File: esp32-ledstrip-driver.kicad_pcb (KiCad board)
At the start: 2 copper layers, 43 parts, among them P1 PWR, P2 LED_1, P3 LED_2, P4 LED_3, P5 LED_4, P6 RS485, Q1 FDD8880?, Q2 FDD8880?, Q3 FDD8880?, Q4 FDD8880?, Q5 FDD8880?, Q6 FDD8880?, Q7 FDD8880?, Q8 FDD8880?, U1 ESP32-WROOM-32, U2 R-78E-1.0, U3 MAX481E

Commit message: first gerbers generated
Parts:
- added C5: 20p, Capacitor_SMD:C_0603_1608Metric, F.Cu at (157.3, 81.7)
- added C6: 20p, Capacitor_SMD:C_0603_1608Metric, F.Cu at (149.7, 81.6)
- added C7: 100n, Capacitor_SMD:C_0603_1608Metric, F.Cu at (151.0, 85.8)
- added C8: 22u, Capacitor_SMD:C_0603_1608Metric, F.Cu at (161.2, 94.7)
- added D2: D_Schottky_Small, Diode_SMD:D_0603_1608Metric_Pad1.05x0.95mm_HandSolder, F.Cu at (160.4, 81.7)
- added D3: D_Schottky_Small, Diode_SMD:D_0603_1608Metric_Pad1.05x0.95mm_HandSolder, F.Cu at (151.2, 92.4)
- added D4: D_Schottky_Small, Diode_SMD:D_0603_1608Metric_Pad1.05x0.95mm_HandSolder, F.Cu at (160.5, 97.5)
- added D5: BAT54C, Package_TO_SOT_SMD:SOT-23, F.Cu at (147.3, 96.1)
- added D6: Led_Small, LED_SMD:LED_0805_2012Metric_Pad1.15x1.40mm_HandSolder, F.Cu at (140.6, 106.3)
- added J1: USB_B_Micro, Connector_USB:USB_Mini-B_Tensility_54-00023_Vertical_CircularHoles, F.Cu at (166.2, 91.2)
- added Q10: BC817, Package_TO_SOT_SMD:SOT-23, F.Cu at (150.8, 96.3)
- added Q9: BC817, Package_TO_SOT_SMD:SOT-23, F.Cu at (157.3, 96.1)
- added R20: 10k, Resistor_SMD:R_0603_1608Metric, F.Cu at (158.9, 81.6)
- added R21: 10k, Resistor_SMD:R_0603_1608Metric, F.Cu at (160.8, 87.8)
- added R22: 1k, Resistor_SMD:R_0603_1608Metric, F.Cu at (154.2, 95.6)
- added R23: 1k, Resistor_SMD:R_0603_1608Metric, F.Cu at (154.2, 97.2)
- added R24: DNP, Resistor_SMD:R_0603_1608Metric, F.Cu at (162.0, 81.6)
- added R25: 220R, Resistor_SMD:R_0603_1608Metric, F.Cu at (148.6, 93.3)
- added R26: 220R, Resistor_SMD:R_0603_1608Metric, F.Cu at (136.8, 106.3)
- added U4: CH340T, Package_SO:SSOP-20_5.3x7.2mm_P0.65mm, F.Cu at (156.0, 89.3)
- added Y1: Crystal_GND24_Small, Crystal:Crystal_SMD_3225-4Pin_3.2x2.5mm_HandSoldering, F.Cu at (153.6, 81.5)
- moved R4 99.4 mm to (70.1, 80.9), turned to 90 degrees
- moved R2 97.1 mm to (71.8, 80.9), turned to -90 degrees
- moved P1 90.0 mm to (69.8, 126.9), turned to 0 degrees
- moved Q2 88.4 mm to (75.1, 75.0), turned to 0 degrees
- moved P2 81.9 mm to (85.3, 61.4), turned to 180 degrees
- moved U2 80.0 mm to (74.0, 111.5), turned to 180 degrees
- moved P3 79.4 mm to (170.6, 61.2), turned to 180 degrees
- moved C2 78.7 mm to (74.5, 106.8), turned to -90 degrees
- moved Q1 74.1 mm to (86.9, 75.0), turned to 180 degrees
- moved L1 70.9 mm to (80.0, 105.8), turned to 180 degrees
- moved D1 69.5 mm to (82.0, 114.6), turned to -90 degrees
- moved R3 66.1 mm to (90.3, 80.2), turned to 90 degrees
- moved R1 64.1 mm to (92.0, 80.2), turned to -90 degrees
- moved R5 63.9 mm to (166.7, 81.2), turned to 90 degrees
- moved P5 63.6 mm to (110.0, 61.5), turned to 180 degrees
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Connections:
- R17 pad 2: Net-(P6-Pad1) -> Net-(P6-Pad3)
- R18 pad 2: Net-(P6-Pad3) -> Net-(P6-Pad1)
- R19 pad 1: Net-(P6-Pad3) -> Net-(P6-Pad1)
- R19 pad 2: Net-(P6-Pad1) -> Net-(P6-Pad3)
- U1 pad 11: unconnected-(U1-Pad11) -> RO
- U1 pad 12: unconnected-(U1-Pad12) -> DI
- U1 pad 24: unconnected-(U1-Pad24) -> GPIO_2
- U1 pad 25: unconnected-(U1-Pad25) -> GPIO_0
- U1 pad 29: unconnected-(U1-Pad29) -> Net-(D6-Pad2)
- U1 pad 3: unconnected-(U1-Pad3) -> ESP_EN
- U1 pad 34: unconnected-(U1-Pad34) -> RXD_0
- U1 pad 35: unconnected-(U1-Pad35) -> TXD_0
- U1 pad 8: unconnected-(U1-Pad8) -> ~{RX}TX
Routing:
- net +24V: track 0.00 -> 199.3 mm
- net +3V3: track 0.00 -> 162.2 mm, vias 0 -> 8
- net LED_1_W: track 0.00 -> 97.1 mm, vias 0 -> 2
- net LED_4_W: track 0.00 -> 86.8 mm, vias 0 -> 4
- net ~{RX}TX: track 0.00 -> 85.4 mm, vias 0 -> 2
- net DI: track 0.00 -> 79.8 mm, vias 0 -> 2
- net LED_1_C: track 0.00 -> 76.2 mm, vias 0 -> 2
- net RXD_0: track 0.00 -> 74.9 mm, vias 0 -> 2
- net RO: track 0.00 -> 73.0 mm, vias 0 -> 2
- net LED_2_C: track 0.00 -> 71.8 mm, vias 0 -> 2
- net LED_4_C: track 0.00 -> 57.1 mm, vias 0 -> 2
- net GND: track 0.00 -> 54.4 mm, vias 0 -> 471
- net TXD_0: track 0.00 -> 51.7 mm
- net LED_3_W: track 0.00 -> 50.4 mm, vias 0 -> 2
- net LED_2_W: track 0.00 -> 49.5 mm, vias 0 -> 2
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- added copper zone on B.Cu, net GND
- added copper zone on F.Cu, net GND
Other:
- board outline added: 160 x 120 mm

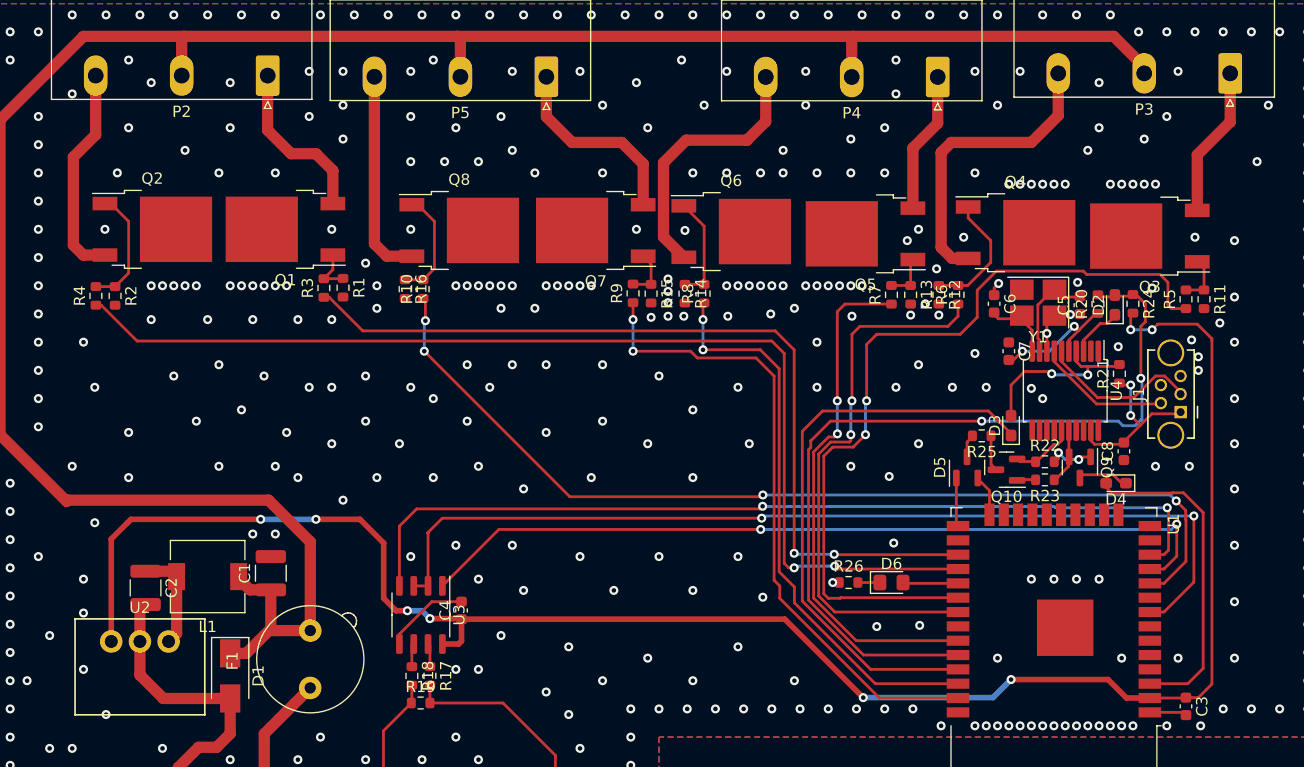
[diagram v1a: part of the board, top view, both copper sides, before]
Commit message: Fixed FET footprints
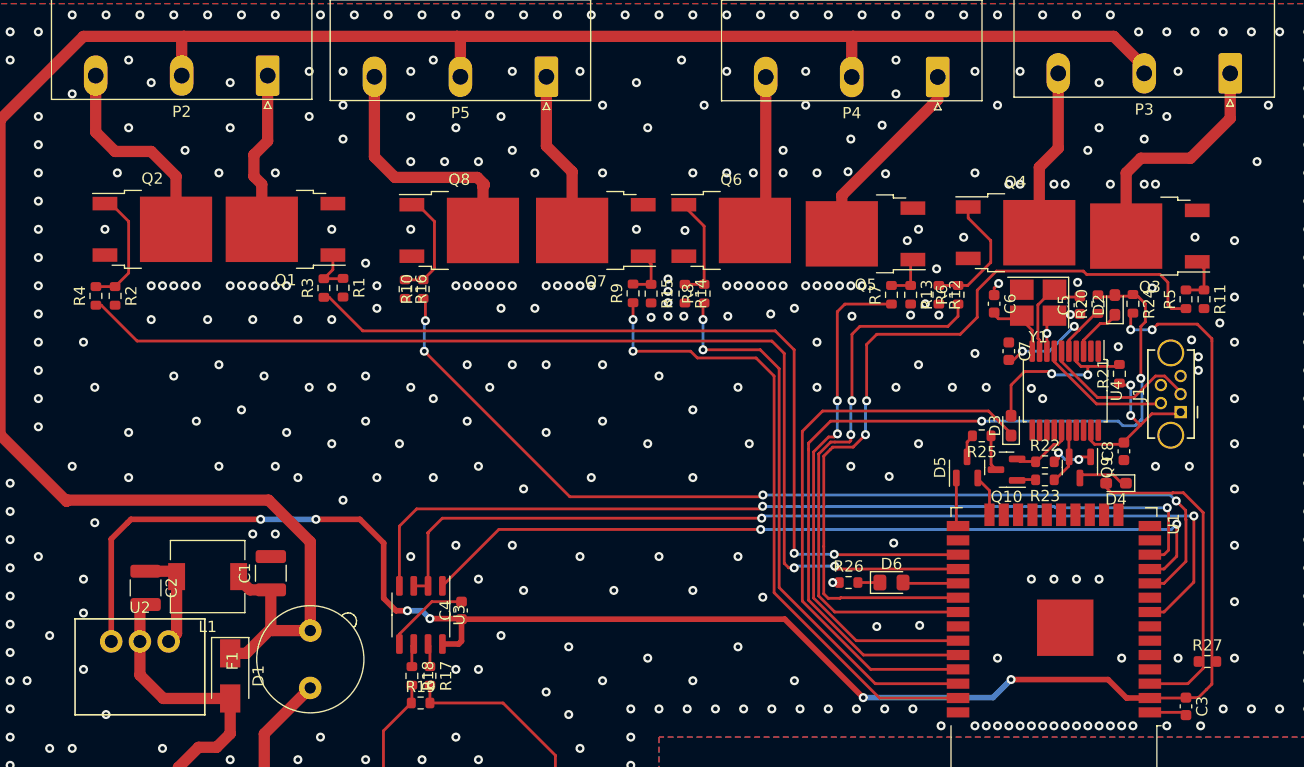
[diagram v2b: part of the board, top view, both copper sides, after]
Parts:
- added R27: 10k, Resistor_SMD:R_0603_1608Metric, F.Cu at (168.6, 113.3)
- Q1, Q2, Q3, Q4, Q5, Q6, Q7, Q8: value FDD8880? -> Q_NMOS_GDS
- moved Q6 0.10 mm to (126.4, 75.1)
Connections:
- Q1 pad 2: GND -> Net-(P2-Pad1)
- Q1 pad 3: Net-(P2-Pad1) -> GND
- Q2 pad 2: GND -> Net-(P2-Pad3)
- Q2 pad 3: Net-(P2-Pad3) -> GND
- Q3 pad 2: GND -> Net-(P3-Pad1)
- Q3 pad 3: Net-(P3-Pad1) -> GND
- Q4 pad 2: GND -> Net-(P3-Pad3)
- Q4 pad 3: Net-(P3-Pad3) -> GND
- Q5 pad 2: GND -> Net-(P4-Pad1)
- Q5 pad 3: Net-(P4-Pad1) -> GND
- Q6 pad 2: GND -> Net-(P4-Pad3)
- Q6 pad 3: Net-(P4-Pad3) -> GND
- Q7 pad 2: GND -> Net-(P5-Pad1)
- Q7 pad 3: Net-(P5-Pad1) -> GND
- Q8 pad 2: GND -> Net-(P5-Pad3)
- Q8 pad 3: Net-(P5-Pad3) -> GND
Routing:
- net Net-(P3-Pad3): track 26.7 -> 14.8 mm
- net Net-(P4-Pad3): track 23.6 -> 14.0 mm
- net Net-(P3-Pad1): track 13.4 -> 20.8 mm
- net Net-(P4-Pad1): track 12.5 -> 17.4 mm
- net Net-(P5-Pad3): track 18.6 -> 22.0 mm
- net Net-(P5-Pad1): track 17.5 -> 14.6 mm
- net Net-(P2-Pad1): track 15.0 -> 14.4 mm
- net Net-(P2-Pad3): track 19.0 -> 18.4 mm
- net GND: vias 471 -> 467
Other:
- board text added: "EN pin needs external pull-up"
- board text added: "MOSFET footprint had D and S swapped"
- board text added: "Mosfet gate drivers?"

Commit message: WIP
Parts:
- added C10: 10u 50V, Capacitor_SMD:C_1210_3225Metric, F.Cu at (97.5, 103.6)
- added C11: 220u, Capacitor_THT:CP_Radial_D8.0mm_P3.50mm, F.Cu at (106.3, 94.8)
- added C9: 100n, Capacitor_SMD:C_0603_1608Metric, F.Cu at (78.7, 87.1)
- added D7: D_Schottky_Small, Diode_SMD:D_SMA, F.Cu at (99.7, 100.2)
- added J2: 1-Wire, TerminalBlock:TerminalBlock_bornier-3_P5.08mm, F.Cu at (177.2, 112.6)
- added J3: Conn_01x08, Connector_PinHeader_2.54mm:PinHeader_1x08_P2.54mm_Vertical, B.Cu at (71.5, 84.7)
- added J4: Conn_01x08, TerminalBlock_Phoenix:TerminalBlock_Phoenix_MKDS-1,5-8-5.08_1x08_P5.08mm_Horizontal, F.Cu at (63.7, 66.7)
- added L2: 68u, Inductor_SMD:L_6.3x6.3_H3, F.Cu at (91.3, 104.4)
- added L3: 330uH, Inductor_SMD:L_6.3x6.3_H3, F.Cu at (99.9, 95.0)
- added Q11: Q_NMOS_GSD_SMALL, Package_TO_SOT_SMD:SOT-23, F.Cu at (112.6, 80.7)
- added Q12: Q_NMOS_GSD_SMALL, Package_TO_SOT_SMD:SOT-23, F.Cu at (103.2, 81.1)
- added Q13: Q_NMOS_GDS, Package_TO_SOT_SMD:TO-252-2, F.Cu at (163.5, 75.6)
- added Q14: Q_NMOS_GDS, Package_TO_SOT_SMD:TO-252-2, F.Cu at (151.6, 75.3)
- added Q15: Q_NMOS_GDS, Package_TO_SOT_SMD:TO-252-2, F.Cu at (138.3, 75.4)
- added Q16: Q_NMOS_GDS, Package_TO_SOT_SMD:TO-252-2, F.Cu at (126.4, 75.0)
- added Q17: Q_NMOS_GDS, Package_TO_SOT_SMD:TO-252-2, F.Cu at (114.5, 75.1)
- added Q18: Q_NMOS_GDS, Package_TO_SOT_SMD:TO-252-2, F.Cu at (102.2, 75.1)
- added R28: 10k, Resistor_SMD:R_0603_1608Metric, F.Cu at (75.7, 87.2)
- added R29: 4k7, Resistor_SMD:R_0603_1608Metric, F.Cu at (79.9, 89.4)
- added R30: 4k7, Resistor_SMD:R_0603_1608Metric, F.Cu at (170.2, 111.8)
- added R31: 4k7, Resistor_SMD:R_0603_1608Metric, F.Cu at (81.5, 89.4)
- added R32: 10k, Resistor_SMD:R_0402_1005Metric, F.Cu at (110.1, 81.2)
- added R33: 10k, Resistor_SMD:R_0402_1005Metric, F.Cu at (104.0, 83.6)
- added R34: 100R, Resistor_SMD:R_0402_1005Metric, F.Cu at (86.7, 80.2)
- added R35: 100R, Resistor_SMD:R_0402_1005Metric, F.Cu at (75.5, 81.1)
- added R36: 100R, Resistor_SMD:R_0402_1005Metric, F.Cu at (169.4, 80.0)
- added R37: 100R, Resistor_SMD:R_0402_1005Metric, F.Cu at (143.8, 82.8)
- added R38: 100R, Resistor_SMD:R_0402_1005Metric, F.Cu at (138.2, 82.1)
- added R39: 100R, Resistor_SMD:R_0402_1005Metric, F.Cu at (125.9, 80.1)
- added R40: 100R, Resistor_SMD:R_0402_1005Metric, F.Cu at (114.8, 81.9)
- added R41: 100R, Resistor_SMD:R_0402_1005Metric, F.Cu at (101.4, 79.9)
- added R42: 1k, Resistor_SMD:R_0402_1005Metric, F.Cu at (87.8, 80.2)
- added R43: 1k, Resistor_SMD:R_0402_1005Metric, F.Cu at (74.4, 81.1)
- added R44: 1k, Resistor_SMD:R_0402_1005Metric, F.Cu at (169.0, 81.7)
- added R45: 1k, Resistor_SMD:R_0402_1005Metric, F.Cu at (143.8, 80.8)
- added R46: 1k, Resistor_SMD:R_0402_1005Metric, F.Cu at (138.2, 80.1)
- added R47: 1k, Resistor_SMD:R_0402_1005Metric, F.Cu at (125.5, 81.8)
- added R48: 1k, Resistor_SMD:R_0402_1005Metric, F.Cu at (115.2, 80.3)
- added R49: 1k, Resistor_SMD:R_0402_1005Metric, F.Cu at (100.8, 81.5)
- added R50: 10k, Resistor_SMD:R_0603_1608Metric, F.Cu at (167.7, 75.6)
- added R51: 10k, Resistor_SMD:R_0603_1608Metric, F.Cu at (147.4, 75.4)
- added R52: 10k, Resistor_SMD:R_0603_1608Metric, F.Cu at (142.6, 75.4)
- added R53: 10k, Resistor_SMD:R_0603_1608Metric, F.Cu at (122.2, 75.0)
- added R54: 10k, Resistor_SMD:R_0603_1608Metric, F.Cu at (118.7, 75.1)
- added R55: 10k, Resistor_SMD:R_0603_1608Metric, F.Cu at (98.1, 75.1)
- added R56: 1k, Resistor_SMD:R_0603_1608Metric, F.Cu at (82.9, 96.3)
- added R57: 7k15, Resistor_SMD:R_0603_1608Metric, F.Cu at (82.9, 93.2)
- added U10: ZXGD3009E6, Package_TO_SOT_SMD:SOT-23-6, F.Cu at (141.0, 81.3)
- added U11: ZXGD3009E6, Package_TO_SOT_SMD:SOT-23-6, F.Cu at (122.8, 81.3)
- added U12: ZXGD3009E6, Package_TO_SOT_SMD:SOT-23-6, F.Cu at (118.0, 80.8)
- added U13: ZXGD3009E6, Package_TO_SOT_SMD:SOT-23-6, F.Cu at (98.2, 80.9)
- added U14: LM2574M-ADJ, Package_SO:SOIC-14W_7.5x9mm_P1.27mm, F.Cu at (89.8, 96.0)
- added U5: PCF8575, Package_SO:SSOP-24_5.3x8.2mm_P0.65mm, F.Cu at (74.3, 92.4)
- added U6: ZXGD3009E6, Package_TO_SOT_SMD:SOT-23-6, F.Cu at (90.5, 80.7)
- added U7: ZXGD3009E6, Package_TO_SOT_SMD:SOT-23-6, F.Cu at (71.7, 80.6)
- added U8: ZXGD3009E6, Package_TO_SOT_SMD:SOT-23-6, F.Cu at (166.3, 81.1)
- added U9: ZXGD3009E6, Package_TO_SOT_SMD:SOT-23-6, F.Cu at (146.4, 81.3)
- P4: value LED_3 -> LED_4
- P5: value LED_4 -> LED_3
- Q3, Q4, Q5, Q6, Q7, Q8: value Q_NMOS_GDS -> Q_NMOS_GSD_SMALL; footprint Package_TO_SOT_SMD:TO-252-2 -> Package_TO_SOT_SMD:SOT-23
- R10, R11, R12, R13, R14, R15, R16, R3, R4, R5, R6, R7, R8, R9: footprint Resistor_SMD:R_0603_1608Metric -> Resistor_SMD:R_0402_1005Metric
- moved R11 86.6 mm to (81.7, 81.6), turned to 90 degrees
- moved Q3 79.4 mm to (84.2, 80.5), turned to 0 degrees
- moved Q4 73.7 mm to (78.0, 80.4), turned to 180 degrees
- moved R12 64.3 mm to (80.5, 79.7)
- moved Q5 33.6 mm to (171.3, 81.3), turned to 90 degrees
- moved R16 33.2 mm to (130.7, 79.8)
- moved R13 29.8 mm to (171.9, 83.8), turned to 180 degrees
- moved R14 26.9 mm to (149.0, 84.2)
- moved Q8 26.4 mm to (128.0, 81.1), turned to 180 degrees
- moved Q6 22.4 mm to (146.5, 84.9), turned to 180 degrees
- moved Q7 22.0 mm to (135.6, 80.9), turned to 0 degrees
- moved R15 13.8 mm to (133.1, 81.8), turned to 90 degrees
- moved R26 10.8 mm to (142.5, 97.1), turned to 90 degrees
- moved R4 10.4 mm to (80.5, 81.6)
- moved D6 10.0 mm to (144.4, 97.0), turned to -90 degrees
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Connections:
- Q1 pad 1: Net-(R1-Pad1) -> Net-(Q1-Pad1)
- Q2 pad 1: Net-(R2-Pad1) -> Net-(Q2-Pad1)
- Q3 pad 1: Net-(R11-Pad1) -> Net-(Q3-Pad1)
- Q3 pad 2: Net-(P3-Pad1) -> GND
- Q3 pad 3: GND -> Net-(Q3-Pad3)
- Q4 pad 1: Net-(R12-Pad1) -> Net-(Q4-Pad1)
- Q4 pad 2: Net-(P3-Pad3) -> GND
- Q4 pad 3: GND -> Net-(Q4-Pad3)
- Q5 pad 1: Net-(R13-Pad1) -> Net-(Q5-Pad1)
- Q5 pad 2: Net-(P4-Pad1) -> GND
- Q5 pad 3: GND -> Net-(Q5-Pad3)
- Q6 pad 1: Net-(R14-Pad1) -> Net-(Q6-Pad1)
- Q6 pad 2: Net-(P4-Pad3) -> GND
- Q6 pad 3: GND -> Net-(Q6-Pad3)
- Q7 pad 1: Net-(R15-Pad1) -> Net-(Q7-Pad1)
- Q7 pad 2: Net-(P5-Pad1) -> GND
- Q7 pad 3: GND -> Net-(Q7-Pad3)
- Q8 pad 1: Net-(R10-Pad2) -> Net-(Q8-Pad1)
- Q8 pad 2: Net-(P5-Pad3) -> GND
- Q8 pad 3: GND -> Net-(Q8-Pad3)
- R1 pad 1: Net-(R1-Pad1) -> Net-(Q1-Pad1)
- R10 pad 1: LED_4_W -> LED_3_W
- R10 pad 2: Net-(R10-Pad2) -> Net-(Q12-Pad1)
- R11 pad 1: Net-(R11-Pad1) -> GND
- R11 pad 2: GND -> Net-(Q3-Pad1)
- R12 pad 1: Net-(R12-Pad1) -> GND
- R12 pad 2: GND -> Net-(Q4-Pad1)
- R13 pad 1: Net-(R13-Pad1) -> GND
- R13 pad 2: GND -> Net-(Q5-Pad1)
- R14 pad 1: Net-(R14-Pad1) -> GND
- R14 pad 2: GND -> Net-(Q6-Pad1)
- R15 pad 1: Net-(R15-Pad1) -> GND
- R15 pad 2: GND -> Net-(Q7-Pad1)
- R16 pad 1: Net-(R10-Pad2) -> GND
- R16 pad 2: GND -> Net-(Q8-Pad1)
- R2 pad 1: Net-(R2-Pad1) -> Net-(Q2-Pad1)
- R3 pad 2: Net-(R1-Pad1) -> Net-(Q3-Pad1)
- R4 pad 2: Net-(R2-Pad1) -> Net-(Q4-Pad1)
- R5 pad 2: Net-(R11-Pad1) -> Net-(Q5-Pad1)
- R6 pad 2: Net-(R12-Pad1) -> Net-(Q6-Pad1)
- R7 pad 1: LED_3_C -> LED_4_C
- R7 pad 2: Net-(R13-Pad1) -> Net-(Q7-Pad1)
- R8 pad 1: LED_3_W -> LED_4_W
- R8 pad 2: Net-(R14-Pad1) -> Net-(Q8-Pad1)
- R9 pad 1: LED_4_C -> LED_3_C
- R9 pad 2: Net-(R15-Pad1) -> Net-(Q11-Pad1)
- U1 pad 16: unconnected-(U1-Pad16) -> LED_3_W
- U1 pad 23: unconnected-(U1-Pad23) -> Net-(D6-Pad2)
- U1 pad 26: unconnected-(U1-Pad26) -> 1-WIRE
- U1 pad 29: Net-(D6-Pad2) -> unconnected-(U1-Pad29)
- U1 pad 33: LED_3_C -> SDA
- U1 pad 36: LED_3_W -> SCL
- U1 pad 6: unconnected-(U1-Pad6) -> ~{IO_INT}
- U1 pad 9: unconnected-(U1-Pad9) -> LED_3_C
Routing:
- net +10V: track 0.00 -> 164.8 mm, vias 0 -> 7
- net ~{IO_INT}: track 0.00 -> 130.3 mm, vias 0 -> 8
- net LED_4_W: track 86.8 -> 0.00 mm, vias 4 -> 0
- net SCL: track 0.00 -> 85.4 mm, vias 0 -> 4
- net SDA: track 0.00 -> 83.8 mm, vias 0 -> 6
- net LED_3_W: track 50.4 -> 0.00 mm, vias 2 -> 0
- net LED_3_C: track 46.0 -> 0.00 mm, vias 2 -> 0
- net Net-(J4-Pad1): track 0.00 -> 45.7 mm
- net 1-WIRE: track 0.00 -> 39.5 mm, vias 0 -> 2
- net +3V3: track 162.2 -> 201.1 mm, vias 8 -> 11
- net Net-(J4-Pad3): track 0.00 -> 34.3 mm
- net +24V: track 199.3 -> 168.3 mm
- net LED_2_C: track 71.8 -> 44.7 mm
- net Net-(J4-Pad5): track 0.00 -> 24.7 mm
- net Net-(J4-Pad7): track 0.00 -> 16.2 mm
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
